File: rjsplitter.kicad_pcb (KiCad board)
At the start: 2 copper layers, 79 x 45.6 mm, 8 parts, among them J1 8P8C, J2 8P8C, J3 8P8C, J4 8P8C, J5 8P8C

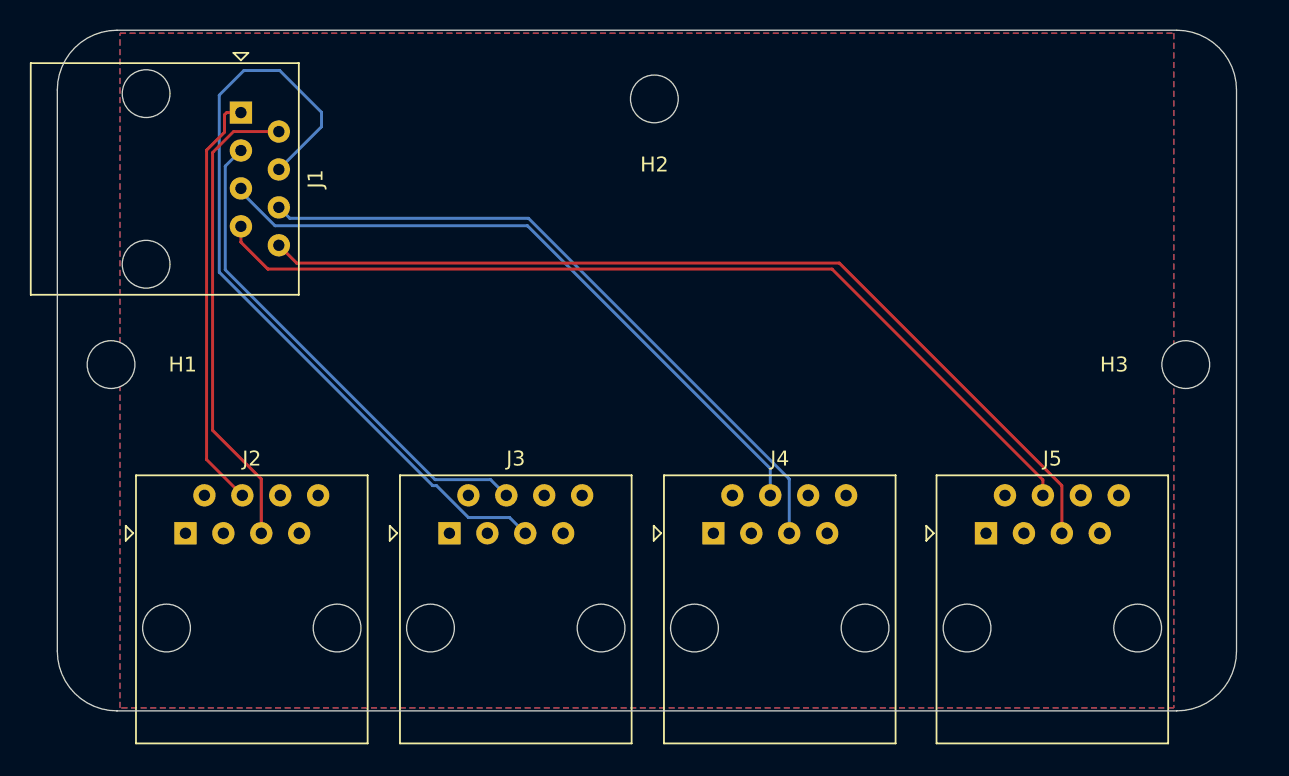
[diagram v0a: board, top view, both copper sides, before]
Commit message: Switch to a mix of RJ45 and RJ11.
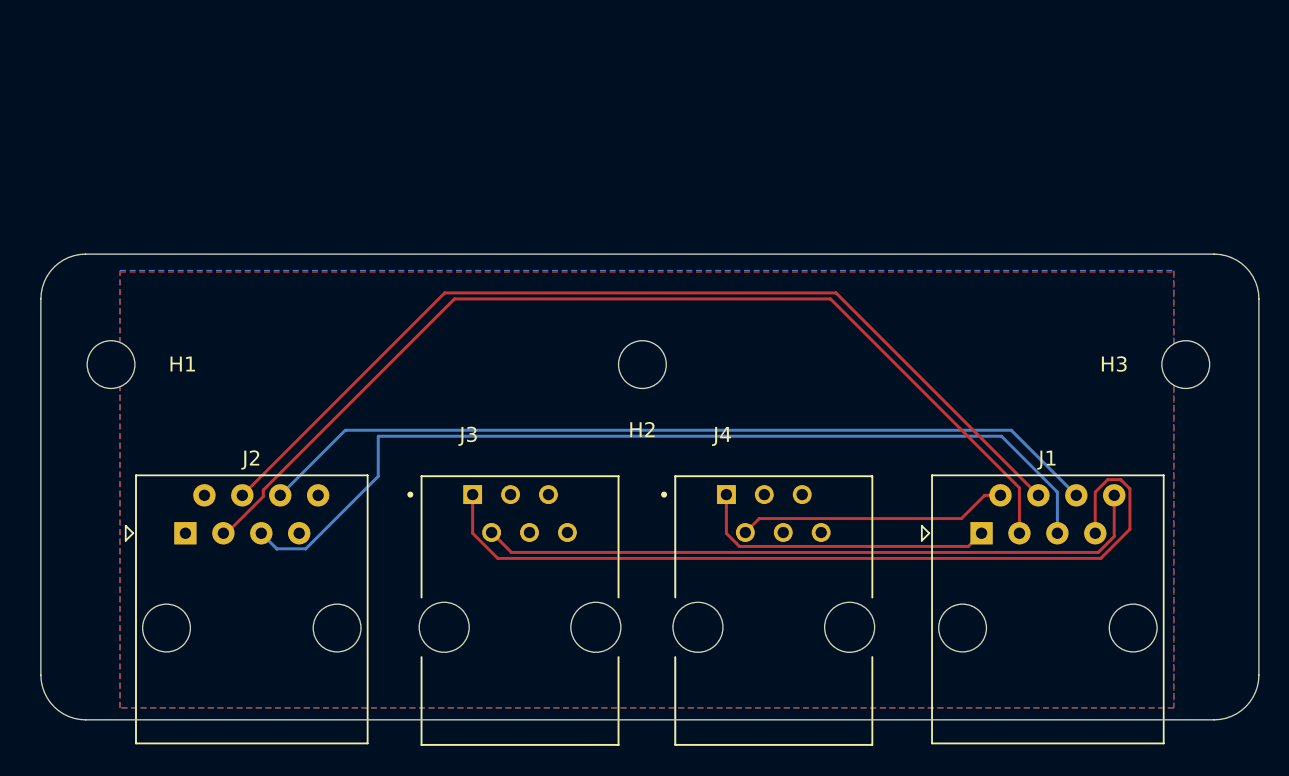
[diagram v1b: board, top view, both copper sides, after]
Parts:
- removed J5: 8P8C, Connector_RJ:RJ45_Amphenol_54602-x08_Horizontal
- J3, J4: value 8P8C -> RJ11; footprint Connector_RJ:RJ45_Amphenol_54602-x08_Horizontal -> kicad:AMPHENOL_54601-906WPLF
- moved J1 57.1 mm to (176.1, 99.9), turned to 0 degrees
- moved H2 17.8 mm to (153.4, 88.6)
- moved J3 7.88 mm to (145.2, 106.2)
- moved J4 7.49 mm to (162.2, 106.2)
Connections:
- J2 pad 3: unconnected-(J2-Pad3) -> Net-(J1-Pad3)
- J2 pad 4: Net-(J1-Pad1) -> Net-(J1-Pad4)
- J2 pad 5: Net-(J1-Pad2) -> Net-(J1-Pad5)
- J2 pad 6: unconnected-(J2-Pad6) -> Net-(J1-Pad6)
- J3 pad 1: unconnected-(J3-Pad1) -> Net-(J1-Pad7)
- J3 pad 2: unconnected-(J3-Pad2) -> Net-(J1-Pad8)
- J3 pad 3: unconnected-(J3-Pad3) -> (no net)
- J3 pad 4: Net-(J1-Pad3) -> (no net)
- J3 pad 5: Net-(J1-Pad4) -> (no net)
- J3 pad 6: unconnected-(J3-Pad6) -> (no net)
- J4 pad 1: unconnected-(J4-Pad1) -> Net-(J1-Pad1)
- J4 pad 2: unconnected-(J4-Pad2) -> Net-(J1-Pad2)
- J4 pad 3: unconnected-(J4-Pad3) -> (no net)
- J4 pad 4: Net-(J1-Pad5) -> (no net)
- J4 pad 5: Net-(J1-Pad6) -> (no net)
- J4 pad 6: unconnected-(J4-Pad6) -> (no net)
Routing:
- net Net-(J1-Pad3): track 33.5 -> 68.4 mm
- net Net-(J1-Pad5): track 45.2 -> 62.8 mm
- net Net-(J1-Pad8): track 62.3 -> 45.5 mm
- net Net-(J1-Pad2): track 31.9 -> 18.1 mm
- net Net-(J1-Pad6): track 45.4 -> 56.9 mm
- net Net-(J1-Pad4): track 53.3 -> 64.6 mm
- net Net-(J1-Pad1): track 28.1 -> 20.4 mm
- net Net-(J1-Pad7): track 62.4 -> 56.5 mm
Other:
- board size 79 x 45.6 mm -> 81.6 x 31.2 mm
